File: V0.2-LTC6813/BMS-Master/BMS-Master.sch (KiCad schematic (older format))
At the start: 26 parts

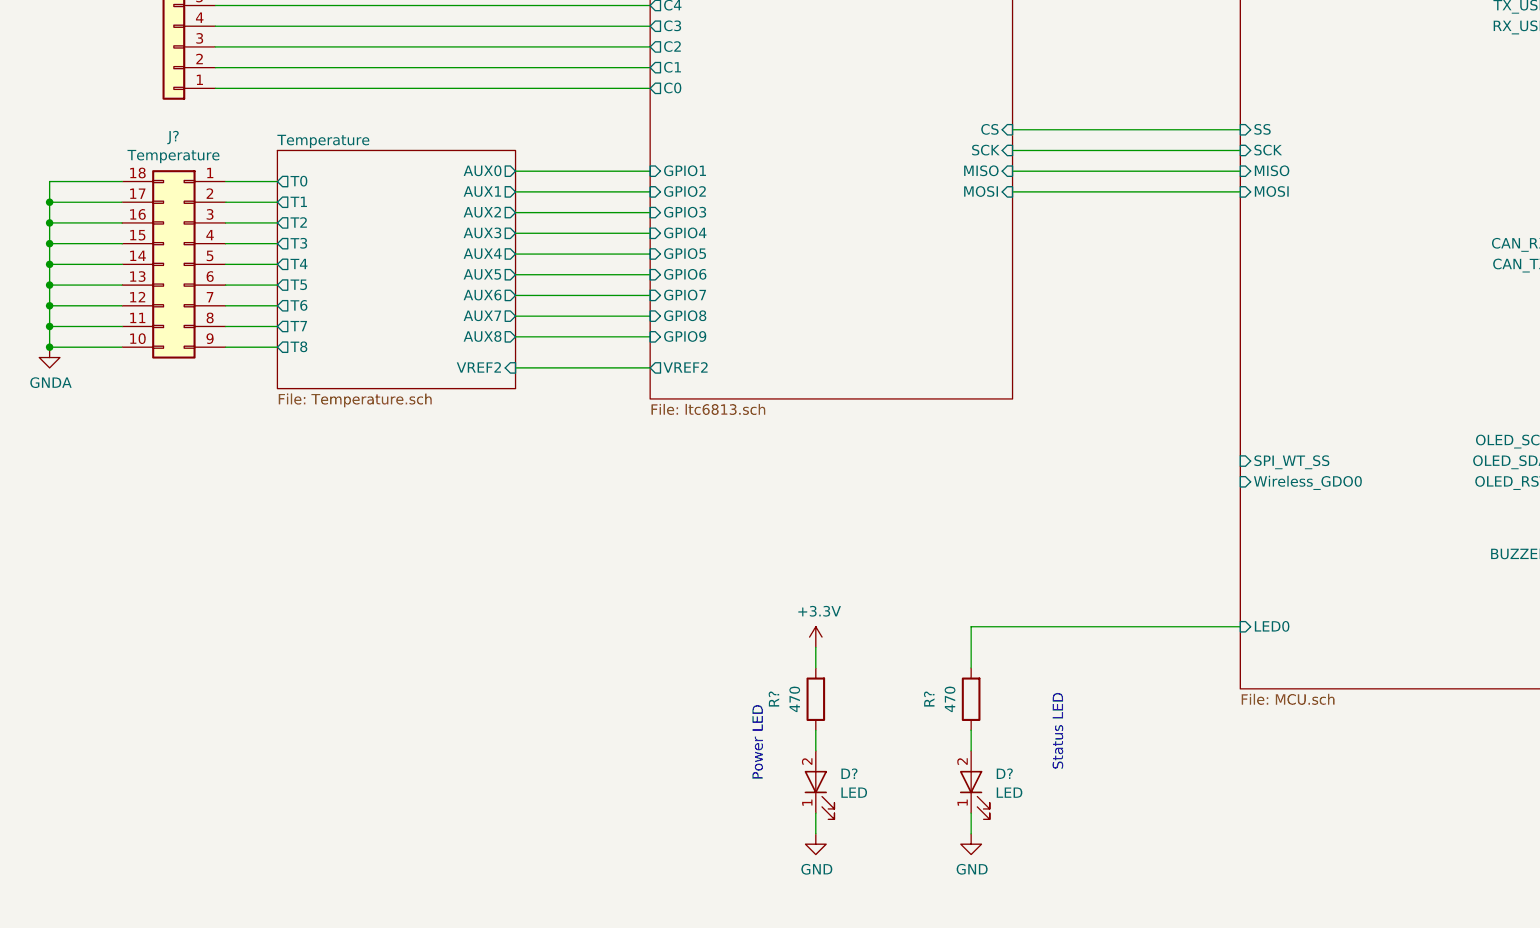
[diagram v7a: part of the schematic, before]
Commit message: Schematics 95% completed
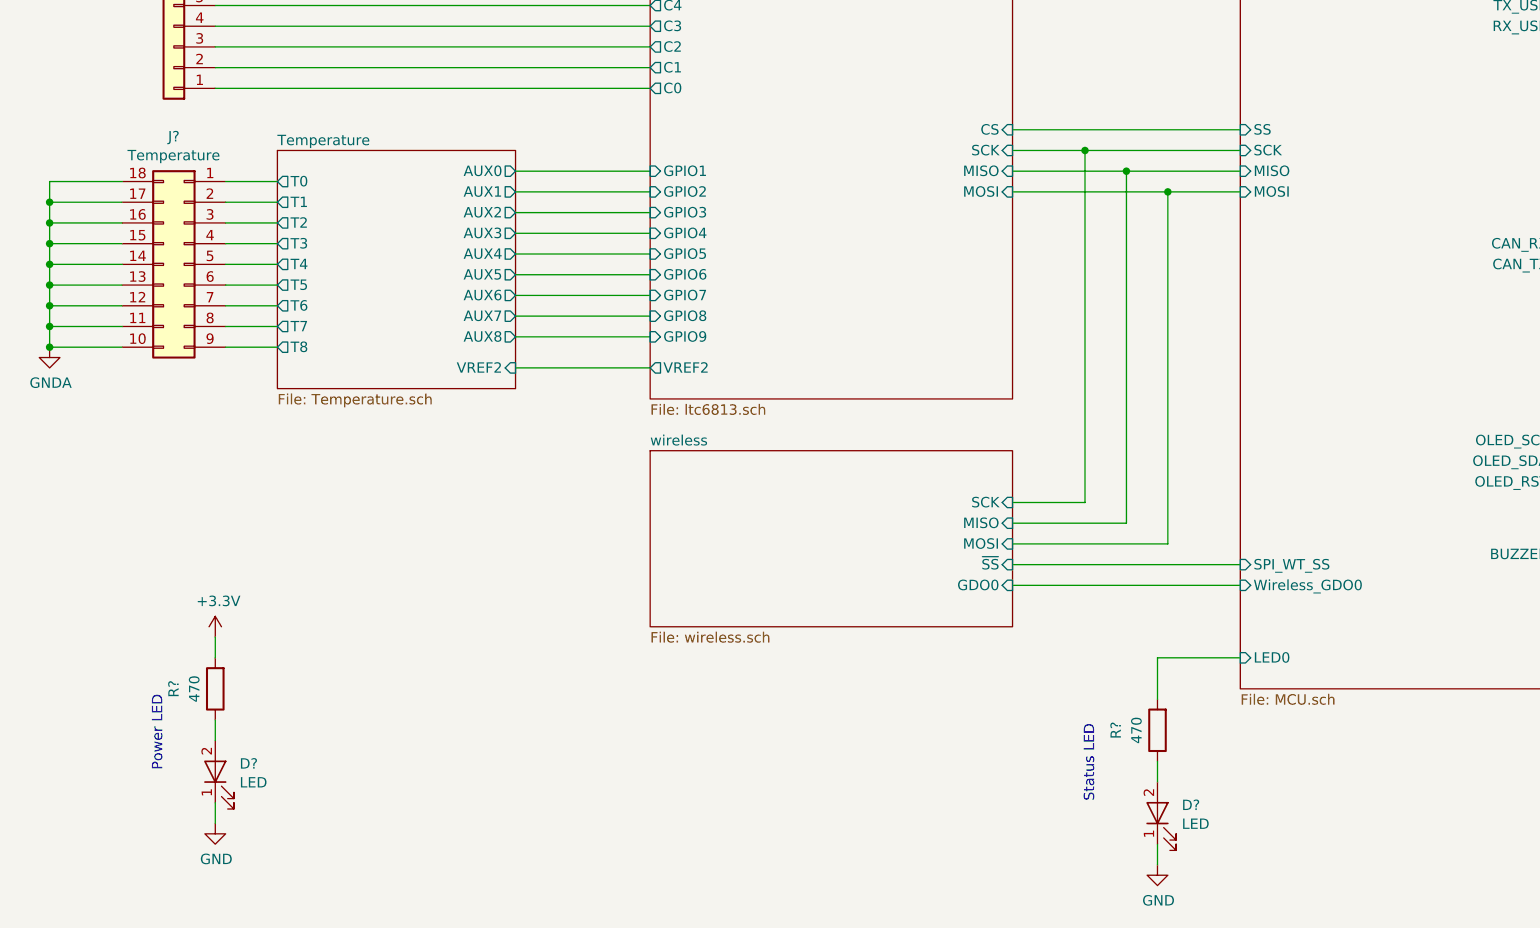
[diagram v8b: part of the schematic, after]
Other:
- moved on the sheet: D?, R?
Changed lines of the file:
@@
 $Descr A3 16535 11693
 encoding utf-8
-Sheet 1 27
+Sheet 1 28
 Title "BMS-Master"
 Date ""
@@
 L BMS-Master-rescue:LED-Device D?
 U 1 1 5ABAB322
-P 5900 10550
-F 0 "D?" V 5938 10433 50  0000 R CNN
-F 1 "LED" V 5847 10433 50  0000 R CNN
-F 2 "LEDs:LED_0603_HandSoldering" H 5900 10550 50  0001 C CNN
-F 3 "~" H 5900 10550 50  0001 C CNN
-	1    5900 10550
+P 6800 10700
+F 0 "D?" V 6838 10583 50  0000 R CNN
+F 1 "LED" V 6747 10583 50  0000 R CNN
+F 2 "LEDs:LED_0603_HandSoldering" H 6800 10700 50  0001 C CNN
+F 3 "~" H 6800 10700 50  0001 C CNN
+	1    6800 10700
 	0    -1   -1   0
 $EndComp
@@
 L BMS-Master-rescue:R-Device R?
 U 1 1 5ABAB411
-P 5900 10150
-F 0 "R?" V 6100 10150 50  0000 C CNN
-F 1 "470" V 6000 10150 50  0000 C CNN
-F 2 "Resistors_SMD:R_0603_HandSoldering" V 5830 10150 50  0001 C CNN
-F 3 "~" H 5900 10150 50  0001 C CNN
-	1    5900 10150
+P 6800 10300
+F 0 "R?" V 7000 10300 50  0000 C CNN
+F 1 "470" V 6900 10300 50  0000 C CNN
+F 2 "Resistors_SMD:R_0603_HandSoldering" V 6730 10300 50  0001 C CNN
+F 3 "~" H 6800 10300 50  0001 C CNN
+	1    6800 10300
 	-1   0    0    1
 $EndComp
@@
 L BMS-Master-rescue:R-Device R?
 U 1 1 5ABB20CA
-P 5150 10150
-F 0 "R?" V 5350 10150 50  0000 C CNN
-F 1 "470" V 5250 10150 50  0000 C CNN
-F 2 "Resistors_SMD:R_0603_HandSoldering" V 5080 10150 50  0001 C CNN
-F 3 "~" H 5150 10150 50  0001 C CNN
-	1    5150 10150
+P 2250 10100
+F 0 "R?" V 2450 10100 50  0000 C CNN
+F 1 "470" V 2350 10100 50  0000 C CNN
+F 2 "Resistors_SMD:R_0603_HandSoldering" V 2180 10100 50  0001 C CNN
+F 3 "~" H 2250 10100 50  0001 C CNN
+	1    2250 10100
 	-1   0    0    1
 $EndComp
@@
 L BMS-Master-rescue:LED-Device D?
 U 1 1 5ABB20FE
-P 5150 10550
-F 0 "D?" V 5188 10433 50  0000 R CNN
-F 1 "LED" V 5097 10433 50  0000 R CNN
-F 2 "LEDs:LED_0603_HandSoldering" H 5150 10550 50  0001 C CNN
-F 3 "~" H 5150 10550 50  0001 C CNN
-	1    5150 10550
+P 2250 10500
+F 0 "D?" V 2288 10383 50  0000 R CNN
+F 1 "LED" V 2197 10383 50  0000 R CNN
+F 2 "LEDs:LED_0603_HandSoldering" H 2250 10500 50  0001 C CNN
+F 3 "~" H 2250 10500 50  0001 C CNN
+	1    2250 10500
 	0    -1   -1   0
 $EndComp
 Wire Wire Line
-	5150 10400 5150 10300
-Wire Wire Line
-	5900 10400 5900 10300
+	2250 10350 2250 10250
+Wire Wire Line
+	6800 10550 6800 10450
 $Comp
 L BMS-Master-rescue:GND-power #PWR?
 U 1 1 5ABB698D
-P 5150 10800
-F 0 "#PWR?" H 5150 10550 50  0001 C CNN
-F 1 "GND" H 5155 10627 50  0000 C CNN
-F 2 "" H 5150 10800 50  0001 C CNN
-F 3 "" H 5150 10800 50  0001 C CNN
-	1    5150 10800
+P 2250 10750
+F 0 "#PWR?" H 2250 10500 50  0001 C CNN
+F 1 "GND" H 2255 10577 50  0000 C CNN
+F 2 "" H 2250 10750 50  0001 C CNN
+F 3 "" H 2250 10750 50  0001 C CNN
+	1    2250 10750
 	1    0    0    -1
 $EndComp
@@
 L BMS-Master-rescue:GND-power #PWR?
 U 1 1 5ABB69D7
-P 5900 10800
-F 0 "#PWR?" H 5900 10550 50  0001 C CNN
-F 1 "GND" H 5905 10627 50  0000 C CNN
-F 2 "" H 5900 10800 50  0001 C CNN
-F 3 "" H 5900 10800 50  0001 C CNN
-	1    5900 10800
-	1    0    0    -1
-$EndComp
-Wire Wire Line
-	5900 10700 5900 10800
-Wire Wire Line
-	5150 10700 5150 10800
-Wire Wire Line
-	5900 10000 5900 9800
-Wire Wire Line
-	5900 9800 7200 9800
+P 6800 10950
+F 0 "#PWR?" H 6800 10700 50  0001 C CNN
+F 1 "GND" H 6805 10777 50  0000 C CNN
+F 2 "" H 6800 10950 50  0001 C CNN
+F 3 "" H 6800 10950 50  0001 C CNN
+	1    6800 10950
+	1    0    0    -1
+$EndComp
+Wire Wire Line
+	6800 10850 6800 10950
+Wire Wire Line
+	2250 10650 2250 10750
+Wire Wire Line
+	6800 10150 6800 9950
 $Comp
 L BMS-Master-rescue:+3.3V-power #PWR?
 U 1 1 5ABBDFF3
-P 5150 9900
-F 0 "#PWR?" H 5150 9750 50  0001 C CNN
-F 1 "+3.3V" H 5165 10073 50  0000 C CNN
-F 2 "" H 5150 9900 50  0001 C CNN
-F 3 "" H 5150 9900 50  0001 C CNN
-	1    5150 9900
-	1    0    0    -1
-$EndComp
-Wire Wire Line
-	5150 9900 5150 10000
-Text Notes 4900 10550 1    50   ~ 0
+P 2250 9850
+F 0 "#PWR?" H 2250 9700 50  0001 C CNN
+F 1 "+3.3V" H 2265 10023 50  0000 C CNN
+F 2 "" H 2250 9850 50  0001 C CNN
+F 3 "" H 2250 9850 50  0001 C CNN
+	1    2250 9850
+	1    0    0    -1
+$EndComp
+Wire Wire Line
+	2250 9850 2250 9950
+Text Notes 2000 10500 1    50   ~ 0
 Power LED
-Text Notes 6350 10500 1    50   ~ 0
+Text Notes 6500 10650 1    50   ~ 0
 Status LED
 $Comp
@@
 	6100 7400 7200 7400
 Wire Wire Line
-	7200 7500 6100 7500
-Wire Wire Line
-	6100 7600 7200 7600
-Wire Wire Line
-	7200 7700 6100 7700
+	7200 7500 6450 7500
+Wire Wire Line
+	6100 7600 6650 7600
+Wire Wire Line
+	7200 7700 6850 7700
 $Sheet
 S 7200 3650 1550 6450
@@
 F6 "PowerButton" I L 7200 4750 50
 F7 "PowerLED" I L 7200 4950 50
-F8 "LED0" I L 7200 9800 50
+F8 "LED0" I L 7200 9950 50
 F9 "ChargeEnable" I L 7200 4100 50
 F10 "CAN_RX" I R 8750 7950 50
@@
 F19 "MISO" I L 7200 7600 50
 F20 "MOSI" I L 7200 7700 50
-F21 "SPI_WT_SS" I L 7200 9000 50
+F21 "SPI_WT_SS" I L 7200 9500 50
 F22 "SCL" I L 7200 4300 50
 F23 "SDA" I L 7200 4400 50
@@
 F25 "OLED_SDA" I R 8750 9000 50
 F26 "OLED_RST" I R 8750 9100 50
-F27 "Wireless_GDO0" I L 7200 9100 50
+F27 "Wireless_GDO0" I L 7200 9600 50
 F28 "SwitchEnable" I L 7200 4000 50
 F29 "NTC_Switch" B R 8750 4200 50
@@
 Wire Wire Line
 	9050 4200 8750 4200
+$Sheet
+S 4350 8950 1750 850
+U 5C8805C1
+F0 "wireless" 50
+F1 "wireless.sch" 50
+F2 "MISO" I R 6100 9300 50
+F3 "MOSI" I R 6100 9400 50
+F4 "SCK" I R 6100 9200 50
+F5 "~SS~" I R 6100 9500 50
+F6 "GDO0" I R 6100 9600 50
+$EndSheet
+Wire Wire Line
+	6800 9950 7200 9950
+Wire Wire Line
+	6100 9600 7200 9600
+Wire Wire Line
+	7200 9500 6100 9500
+Wire Wire Line
+	6100 9200 6450 9200
+Wire Wire Line
+	6450 9200 6450 7500
+Connection ~ 6450 7500
+Wire Wire Line
+	6450 7500 6100 7500
+Wire Wire Line
+	6650 9300 6650 7600
+Connection ~ 6650 7600
+Wire Wire Line
+	6650 7600 7200 7600
+Wire Wire Line
+	6100 9400 6850 9400
+Wire Wire Line
+	6850 9400 6850 7700
+Connection ~ 6850 7700
+Wire Wire Line
+	6850 7700 6100 7700
+Wire Wire Line
+	6100 9300 6650 9300
 $EndSCHEMATC
